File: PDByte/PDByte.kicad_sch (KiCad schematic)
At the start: 15 parts, among them J1 Battery1, J10 Motor 7, J11 Motor 8, J12 Motor 9, J13 Motor 10, J14 Motor 11, J15 Motor 12, J2 Battery2, J3 Motor 1, J4 Motor 2, J5 Motor 3, J6 Motor 4, J7 Motor 5, J8 Motor 6, J9 Conn_01x02

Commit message: corrections
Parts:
- removed J10: Motor 7, symbol Connector_Generic:Conn_01x02
- removed J11: Motor 8, symbol Connector_Generic:Conn_01x02
- removed J12: Motor 9, symbol Connector_Generic:Conn_01x02
- removed J9: Conn_01x02, symbol Connector_Generic:Conn_01x02
- added C1, C10, C11, C12, C2, C3, C4, C5, C6, C7, C8, C9: 330uF, symbol Device:C_Polarized_Small
- added J16: Motor 10, symbol Connector_Generic:Conn_01x02
- added J17: Motor 11, symbol Connector_Generic:Conn_01x02
- added J18: Motor 12, symbol Connector_Generic:Conn_01x02
- J1: footprint (none) -> Connector_AMASS:AMASS_XT90PW-M_1x02_P10.90mm_Horizontal
- J13: value Motor 10 -> Motor 7
- J14: value Motor 11 -> Motor 8
- J15: value Motor 12 -> Motor 9
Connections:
- net +48V: now also J13.2 (Pin_2), J14.2 (Pin_2), J15.2 (Pin_2), C1.1, C10.1, C11.1, C12.1, C2.1, C3.1, C4.1, C5.1, C6.1, C7.1, C8.1, C9.1, J16.1 (Pin_1), J17.1 (Pin_1), J18.1 (Pin_1); no longer J13.1 (Pin_1), J14.1 (Pin_1), J15.1 (Pin_1)
- net GND: now also J13.1 (Pin_1), J14.1 (Pin_1), J15.1 (Pin_1), C1.2, C10.2, C11.2, C12.2, C2.2, C3.2, C4.2, C5.2, C6.2, C7.2, C8.2, C9.2, J16.2 (Pin_2), J17.2 (Pin_2), J18.2 (Pin_2); no longer J13.2 (Pin_2), J14.2 (Pin_2), J15.2 (Pin_2)
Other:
- note added: "Actuators power connection"
- note removed: "Actuators connection"
- moved on the sheet: J1, J2, J3, J4, J5, J6, J7, J8

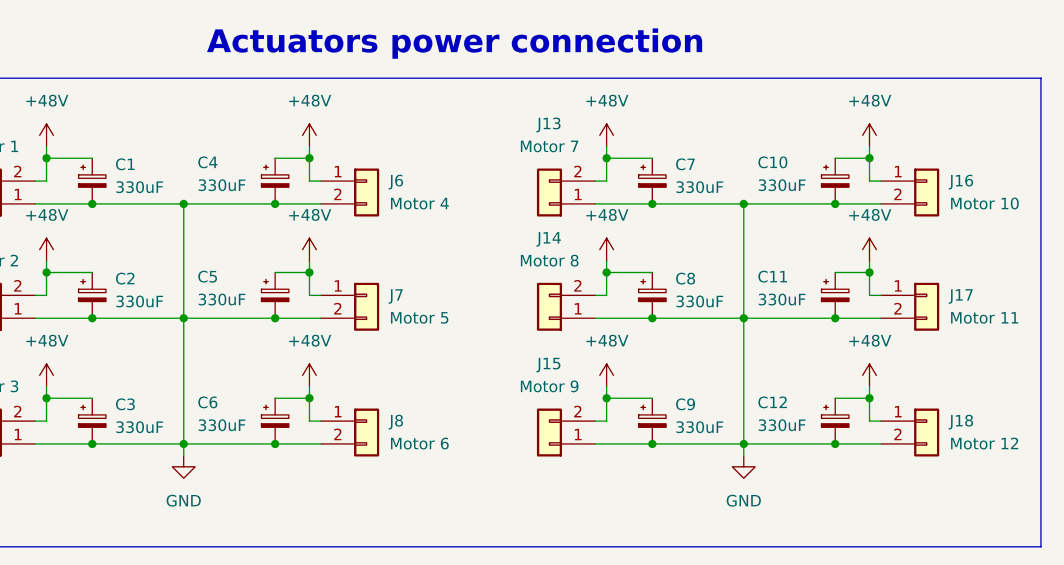
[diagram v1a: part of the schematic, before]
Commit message: corrected Electrical scheme with conventions
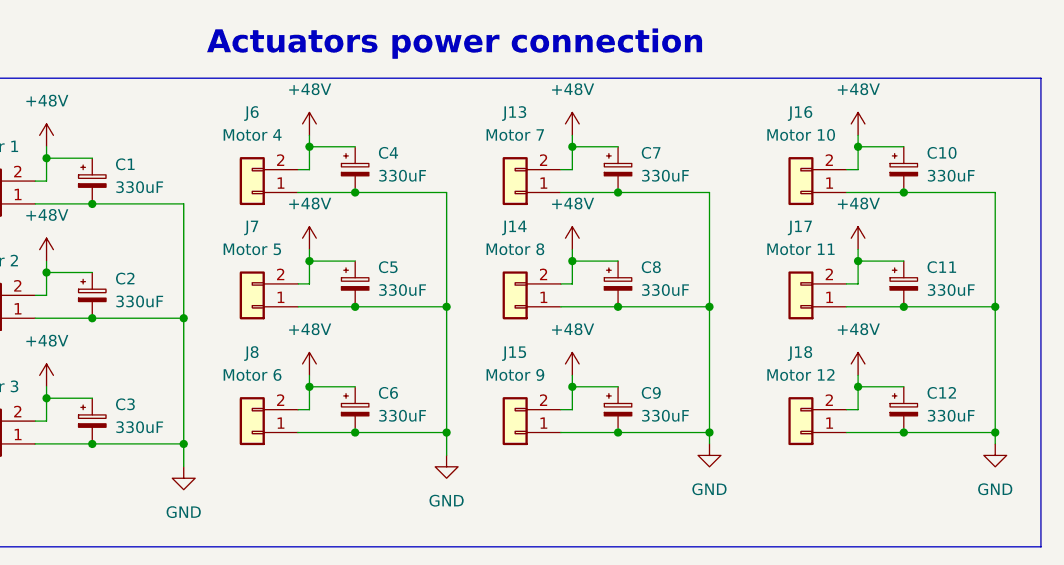
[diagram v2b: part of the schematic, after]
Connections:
- net +48V: now also J16.2 (Pin_2), J17.2 (Pin_2), J18.2 (Pin_2), J6.2 (Pin_2), J7.2 (Pin_2), J8.2 (Pin_2); no longer J16.1 (Pin_1), J17.1 (Pin_1), J18.1 (Pin_1), J6.1 (Pin_1), J7.1 (Pin_1), J8.1 (Pin_1)
- net GND: now also J16.1 (Pin_1), J17.1 (Pin_1), J18.1 (Pin_1), J6.1 (Pin_1), J7.1 (Pin_1), J8.1 (Pin_1); no longer J16.2 (Pin_2), J17.2 (Pin_2), J18.2 (Pin_2), J6.2 (Pin_2), J7.2 (Pin_2), J8.2 (Pin_2)
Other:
- moved on the sheet: C7, C8, C9, J13, J14, J15
